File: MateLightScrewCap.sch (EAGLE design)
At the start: 3 parts, among them X1 PHOENIX-1778780, X3 PHOENIX-1778780

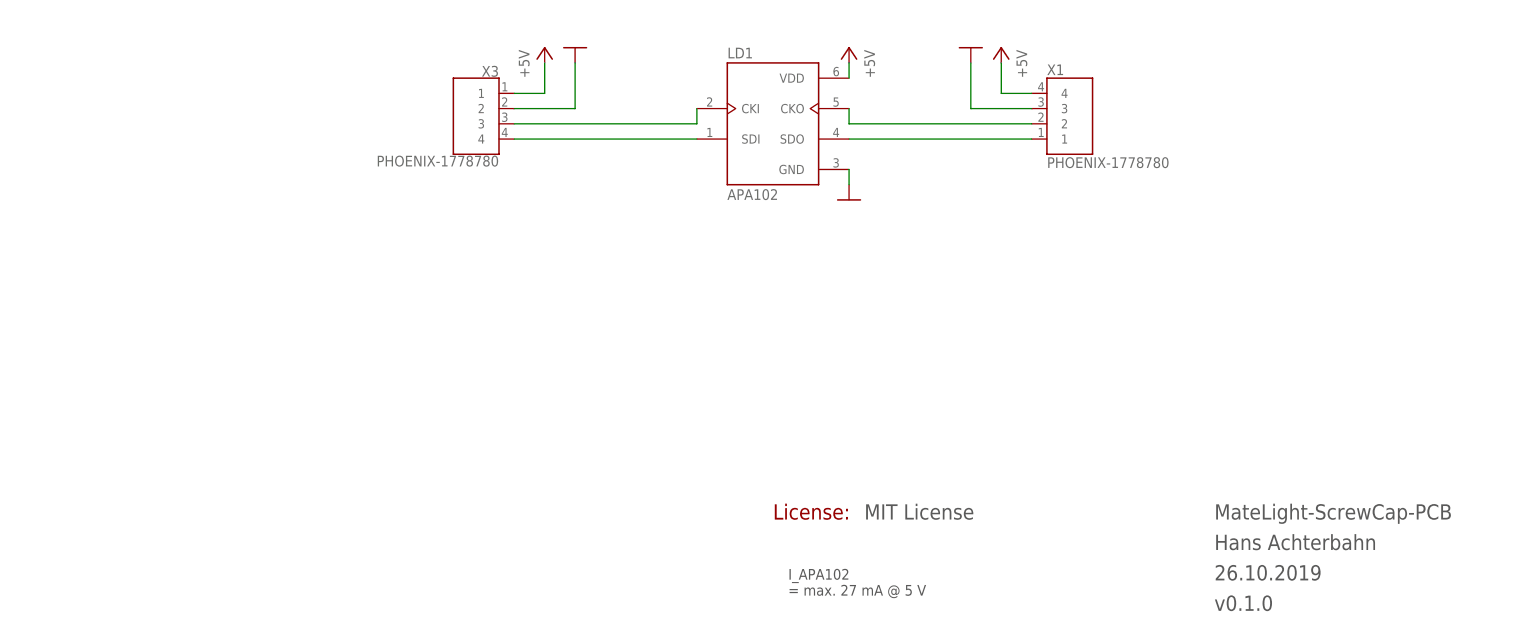
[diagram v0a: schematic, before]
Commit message: Connector getauscht: Phoenix-1778780 → JST S4B-PH-SM4-TB
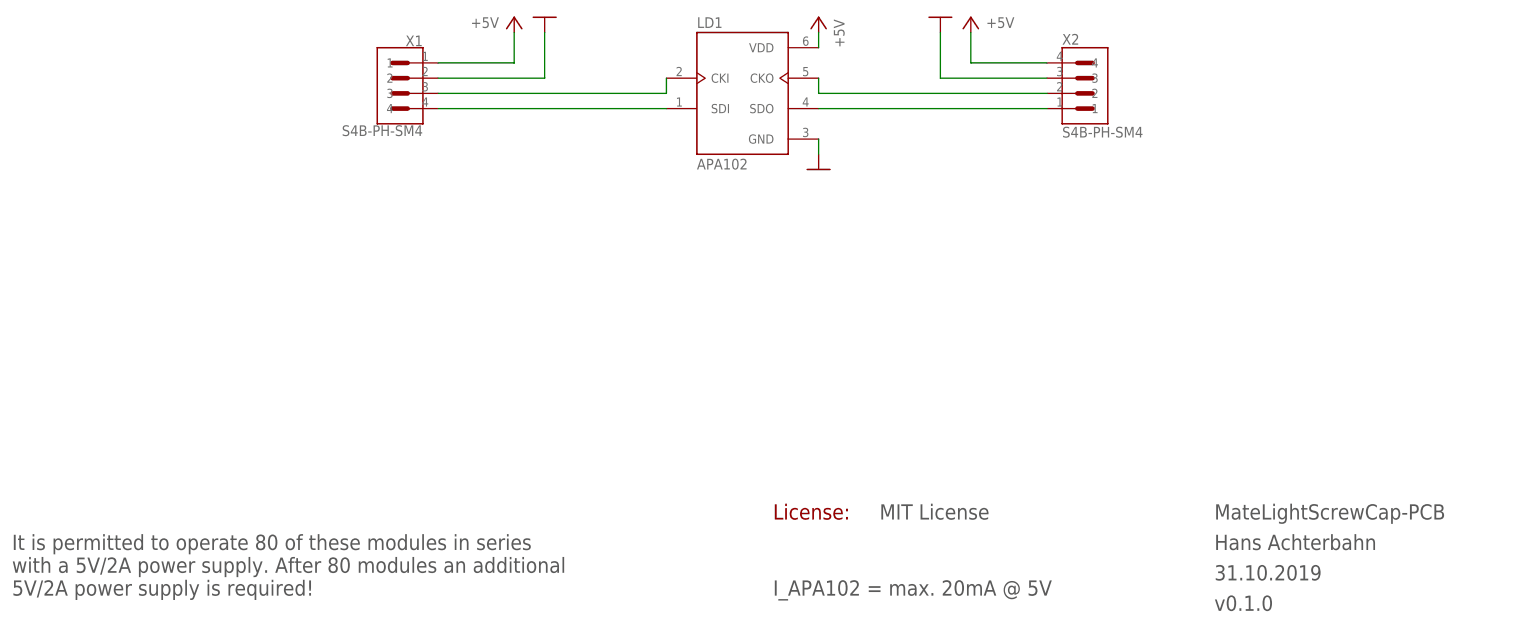
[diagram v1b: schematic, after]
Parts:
- removed X3: PHOENIX-1778780, h8-conector:PHOENIX-1778780
- added X2: S4B-PH-SM4, h8-connector:S4B-PH-SM4-TB
- X1: value PHOENIX-1778780 -> S4B-PH-SM4; device h8-conector:PHOENIX-1778780 -> h8-connector:S4B-PH-SM4-TB
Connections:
- removed net LED-SPI-CLK: LD1.CKI, X3.3
- removed net LED-SPI-MOSI: LD1.SDI, X3.4
- removed net N$37: LD1.CKO, X1.2
- removed net N$39: LD1.SDO, X1.1
- new net LED-SPI-CLK-IN: LD1.CKI, X1.3
- new net LED-SPI-CLK-OUT: LD1.CKO, X2.2
- new net LED-SPI-MOSI-IN: LD1.SDI, X1.4
- new net LED-SPI-MOSI-OUT: LD1.SDO, X2.1
- net +5V: now also X1.1, X2.4; no longer X1.4, X3.1
- net GND: now also X1.2, X2.3; no longer X1.3, X3.2
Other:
- note added: "I_APA102 = max. 20mA @ 5V"
- note added: "It is permitted to operate 80 of these modules in series with a 5V/2A power supply. After 80 modules an additional 5V/2A power supply is required!"
- note removed: "I_APA102 = max. 27 mA @ 5 V"
- moved on the sheet: LD1

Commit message: Repaired document consistency | correct current source properties
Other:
- note added: "It is permitted to operate 20 of these modules in series with a 5V/1.4A power supply. After 20 modules an additional 5V/1.4A power supply is required!"
- note removed: "It is permitted to operate 80 of these modules in series with a 5V/2A power supply. After 80 modules an additional 5V/2A power supply is required!"
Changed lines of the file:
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@@
 </classes>
 <parts>
-<part name="FRAME3" library="h8-frame" library_urn="urn:adsk.eagle:library:13329330" deviceset="A4L-LOC" device=""/>
+<part name="FRAME" library="h8-frame" library_urn="urn:adsk.eagle:library:13329330" deviceset="A4L-LOC" device=""/>
 <part name="LD1" library="h8-optic" library_urn="urn:adsk.eagle:library:11858716" deviceset="APA102" device="APA102C-5050" package3d_urn="urn:adsk.eagle:package:11858725/2" value="APA102"/>
 <part name="GND15" library="supply1" library_urn="urn:adsk.eagle:library:371" deviceset="GND" device=""/>
@@
 <text x="152.4" y="20.32" size="2.54" layer="97" font="vector">&gt;LICENSE</text>
 <text x="134.62" y="20.32" size="2.54" layer="94" font="vector">License:</text>
-<text x="7.62" y="7.62" size="2.54" layer="97" font="vector">It is permitted to operate 80 of these modules in series
-with a 5V/2A power supply. After 80 modules an additional
-5V/2A power supply is required!</text>
+<text x="7.62" y="7.62" size="2.54" layer="97" font="vector">It is permitted to operate 20 of these modules in series
+with a 5V/1.4A power supply. After 20 modules an
+additional 5V/1.4A power supply is required!</text>
 </plain>
 <instances>
-<instance part="FRAME3" gate="G$1" x="0" y="0" smashed="yes">
+<instance part="FRAME" gate="G$1" x="0" y="0" smashed="yes">
 <attribute name="SHEET" x="254" y="5.08" size="2.54" layer="94" font="vector" rot="MR0"/>
 </instance>
